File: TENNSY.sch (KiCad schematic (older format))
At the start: 24 parts, among them J1 HEADER_2, J2 HEADER_2, U1 Teensy4.0, U2 DRV8872, U3 QRE1113, U4 QRE1113, U5 QRE1113, U6 QRE1113, U7 QRE1113, U8 DRV8872

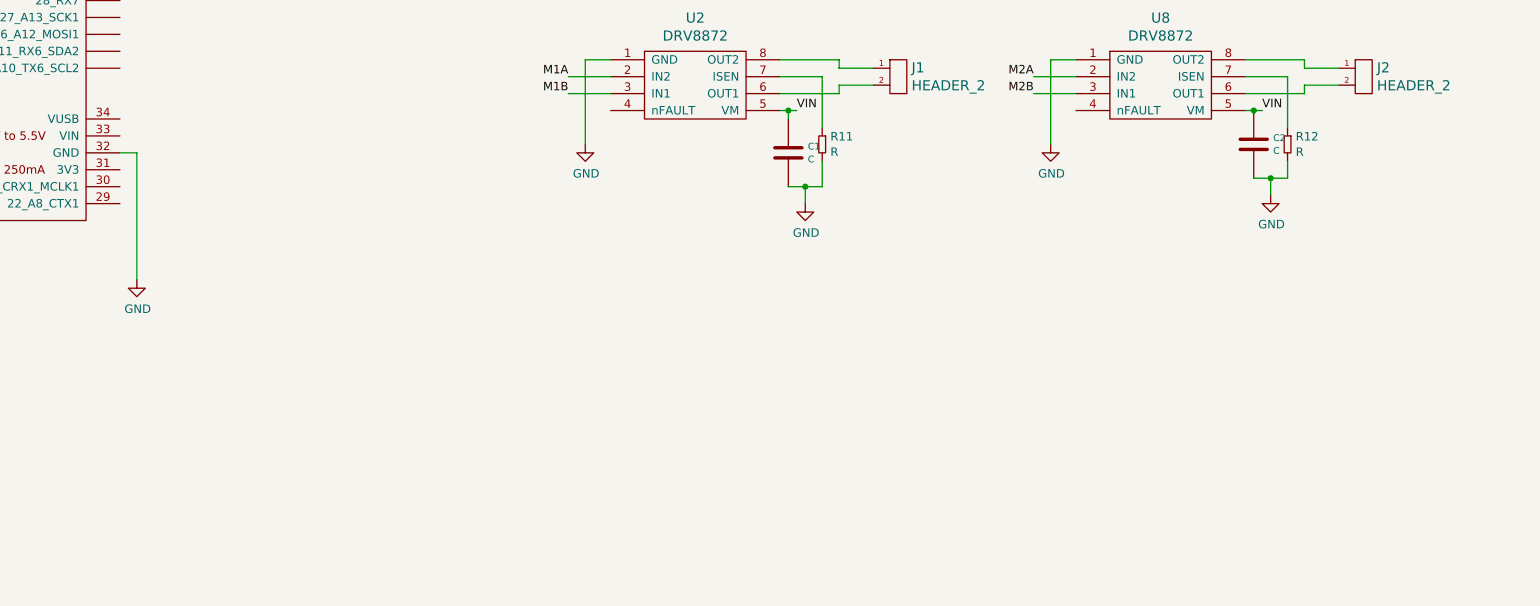
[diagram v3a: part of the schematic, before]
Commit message: modificaciones
se modifico sch,pcb:
se agrego una llave
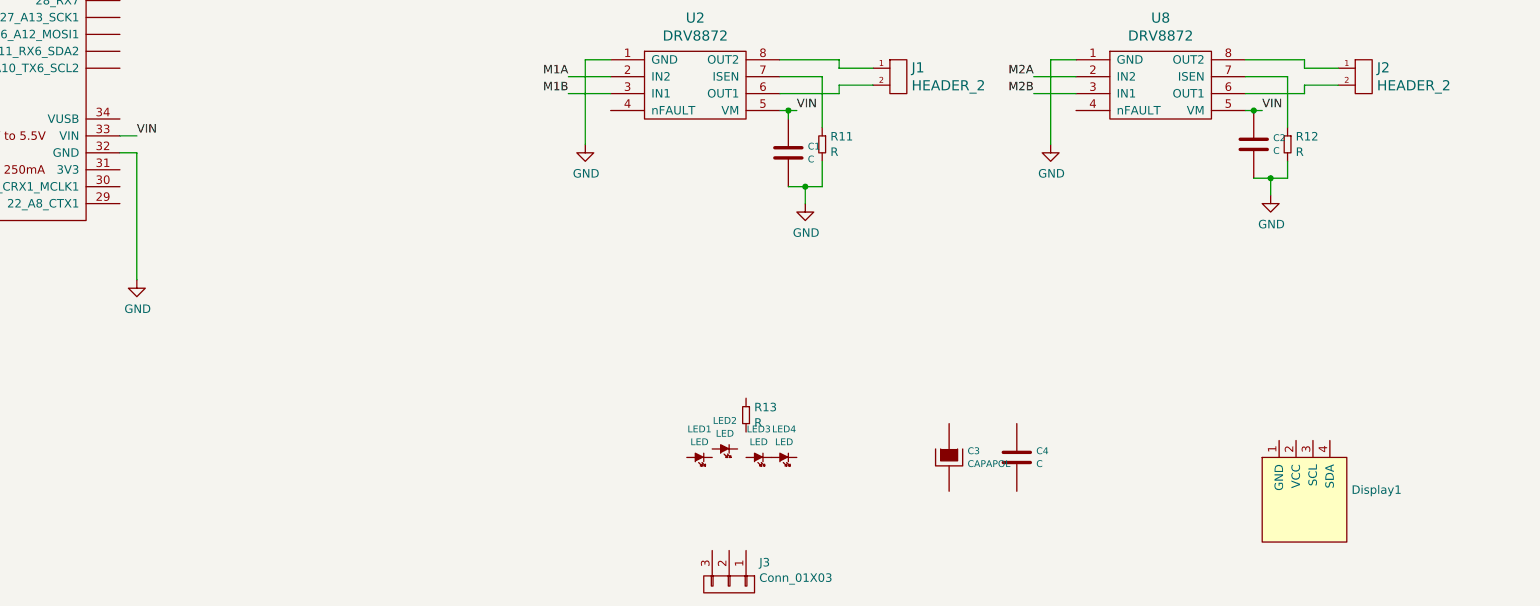
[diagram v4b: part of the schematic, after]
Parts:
- added C3: CAPAPOL, symbol EESTN5:CAPAPOL
- added C4: C, symbol EESTN5:C
- added Display1: SSD1306-SSD1306-128x64_OLED, EESTN5:128x64OLED, symbol EESTN5:SSD1306-SSD1306-128x64_OLED
- added J3: Conn_01X03, Button_Switch_SMD:SW_SPDT_PCM12, symbol EESTN5:Conn_01X03
- added LED1, LED2, LED3, LED4: LED, symbol EESTN5:LED
- added R13: R, symbol EESTN5:R
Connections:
- net VIN: now also U1.33 (VIN)
- new net: LED3.2 (K), LED4.1 (A)
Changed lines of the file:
@@
 Wire Wire Line
 	9950 3200 10000 3200
+Wire Wire Line
+	3250 3350 3350 3350
+Text Label 3350 3350 0    50   ~ 0
+VIN
+$Comp
+L EESTN5:SSD1306-SSD1306-128x64_OLED Display1
+U 1 1 60E7DE53
+P 10250 5500
+F 0 "Display1" H 10528 5558 50  0000 L CNN
+F 1 "SSD1306-SSD1306-128x64_OLED" H 10250 5450 50  0001 C CNN
+F 2 "EESTN5:128x64OLED" H 10250 5750 50  0001 C CNN
+F 3 "" H 10250 5750 50  0001 C CNN
+	1    10250 5500
+	1    0    0    -1
+$EndComp
+$Comp
+L EESTN5:C C4
+U 1 1 60E7E7AF
+P 8550 5250
+F 0 "C4" H 8665 5288 40  0000 L CNN
+F 1 "C" H 8665 5212 40  0000 L CNN
+F 2 "" H 8588 5100 30  0001 C CNN
+F 3 "" H 8550 5250 60  0000 C CNN
+	1    8550 5250
+	1    0    0    -1
+$EndComp
+$Comp
+L EESTN5:CAPAPOL C3
+U 1 1 60E7EE1B
+P 8150 5250
+F 0 "C3" H 8259 5288 40  0000 L CNN
+F 1 "CAPAPOL" H 8259 5212 40  0000 L CNN
+F 2 "" H 8250 5100 30  0001 C CNN
+F 3 "" H 8150 5250 300 0000 C CNN
+	1    8150 5250
+	1    0    0    -1
+$EndComp
+$Comp
+L EESTN5:LED LED1
+U 1 1 60E7F5B7
+P 6650 5250
+F 0 "LED1" H 6675 5417 40  0000 C CNN
+F 1 "LED" H 6675 5341 40  0000 C CNN
+F 2 "" H 6650 5250 60  0001 C CNN
+F 3 "" H 6650 5250 60  0000 C CNN
+	1    6650 5250
+	1    0    0    -1
+$EndComp
+$Comp
+L EESTN5:R R13
+U 1 1 60E7FA33
+P 6950 5000
+F 0 "R13" H 6998 5046 50  0000 L CNN
+F 1 "R" H 6998 4955 50  0000 L CNN
+F 2 "" H 6950 5000 60  0001 C CNN
+F 3 "" H 6950 5000 60  0000 C CNN
+	1    6950 5000
+	1    0    0    -1
+$EndComp
+$Comp
+L EESTN5:LED LED2
+U 1 1 60E80025
+P 6800 5200
+F 0 "LED2" H 6825 5367 40  0000 C CNN
+F 1 "LED" H 6825 5291 40  0000 C CNN
+F 2 "" H 6800 5200 60  0001 C CNN
+F 3 "" H 6800 5200 60  0000 C CNN
+	1    6800 5200
+	1    0    0    -1
+$EndComp
+$Comp
+L EESTN5:LED LED3
+U 1 1 60E80C4D
+P 7000 5250
+F 0 "LED3" H 7025 5417 40  0000 C CNN
+F 1 "LED" H 7025 5341 40  0000 C CNN
+F 2 "" H 7000 5250 60  0001 C CNN
+F 3 "" H 7000 5250 60  0000 C CNN
+	1    7000 5250
+	1    0    0    -1
+$EndComp
+$Comp
+L EESTN5:LED LED4
+U 1 1 60E814F3
+P 7150 5250
+F 0 "LED4" H 7175 5417 40  0000 C CNN
+F 1 "LED" H 7175 5341 40  0000 C CNN
+F 2 "" H 7150 5250 60  0001 C CNN
+F 3 "" H 7150 5250 60  0000 C CNN
+	1    7150 5250
+	1    0    0    -1
+$EndComp
+$Comp
+L EESTN5:Conn_01X03 J3
+U 1 1 60E81E46
+P 6850 6000
+F 0 "J3" V 6721 6178 50  0000 L CNN
+F 1 "Conn_01X03" V 6812 6178 50  0000 L CNN
+F 2 "Button_Switch_SMD:SW_SPDT_PCM12" H 6850 6000 50  0001 C CNN
+F 3 "" H 6850 6000 50  0001 C CNN
+	1    6850 6000
+	0    1    1    0
+$EndComp
 $EndSCHEMATC

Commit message: MODIFICACIONES
se modifico el sch y pcb
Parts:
- added J4: TB_1X2, EESTN5:BORNERA2_DUO, symbol EESTN5:TB_1X2
- added Q1, Q2, Q3: 2N7002, EESTN5:SOT23, symbol EESTN5:2N7002
- added R14, R15, R16, R17, R18, R19, R20, R21: R, EESTN5:R_1206, symbol EESTN5:R
- added SW1: SW_DIP_x02, EESTN5:DIP-4_PC817, symbol EESTN5:SW_DIP_x02
- C3: footprint (none) -> EESTN5:CAP_ELEC_SMD_4X5.5
- C4: footprint (none) -> EESTN5:C_1206
- LED1, LED2, LED3, LED4: footprint (none) -> EESTN5:LED_1206
- R13: footprint (none) -> EESTN5:R_1206
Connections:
- net GND: now also C3.2, C4.2, Display1.1 (GND), R13.2, J4.1, Q1.3 (S), Q2.3 (S), Q3.3 (S), R15.2, R16.2, R18.2, SW1.3, SW1.4
- net M1A: now also U1.4 (2_OUT2)
- net M1B: now also U1.5 (3_LRCLK2)
- net M2A: now also U1.7 (5_IN2)
- net M2B: now also U1.8 (6_OUT1D)
- net MODO2: now reaches U1.10 (8_TX2_IN1)
- net MODO2: now also Q2.1 (G), R16.1
- net MODO3: now reaches U1.11 (9_OUT1C)
- net MODO3: now also Q3.1 (G), R18.1
- net SDA: now reaches U1.25 (18_A4_SDA0)
- net SDA: now also Display1.4 (SDA)
- net SCL: now reaches U1.26 (19_A5_SCL0)
- net SCL: now also Display1.3 (SCL)
- net MODE1: now reaches U1.9 (7_RX2_OUT1A)
- net MODE1: now also R13.1, Q1.1 (G)
- net VCC: now reaches Display1.2 (VCC)
- net VCC: now also LED1.2 (K), LED2.2 (K), LED4.2 (K), R20.1, R21.1
- net at C4.1: now also C3.1, J3.1 (P1), LED3.1 (A)
- net at LED1.1 (A): now also R19.1
- net at LED2.1 (A): now also R17.1
- net at LED3.2 (K): now also R15.1; no longer LED4.1 (A)
- net at J3.2 (P2): now also J3.3 (P3), J4.2
- new net: LED4.1 (A), R14.1
- new net: Q1.2 (D), R14.2
- new net: Q2.2 (D), R17.2
- new net: Q3.2 (D), R19.2
- new net ESTRATEGIAS1: R20.2, SW1.2
- new net ESTRATEGIAS2: R21.2, SW1.1
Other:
- moved on the sheet: C3, C4, Display1, J3, LED1, LED2, LED3, LED4, R13

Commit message: modificaciones
se realizo modificaciones en el sch y pcb, proyecto en su 70% para su finalizacion
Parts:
- added C5: C, EESTN5:C_1206, symbol EESTN5:C
- added U9: LM1117-SOT, EESTN5:SOT223, symbol EESTN5:LM1117-SOT
- J3: footprint Button_Switch_SMD:SW_SPDT_PCM12 -> EESTN5:Pin_Strip_3
- SW1: footprint EESTN5:DIP-4_PC817 -> EESTN5:Dip_SW_2-300
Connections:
- net GND: now also C5.2, U9.1 (ADJ/GND)
- net M1A: now also U2.3 (IN1); no longer U2.2 (IN2)
- net M1B: now also U2.2 (IN2); no longer U2.3 (IN1)
- net M2A: now also U8.3 (IN1); no longer U8.2 (IN2)
- net M2B: now also U8.2 (IN2); no longer U8.3 (IN1)
- net VCC: now also U1.33 (VIN), C5.1, U9.2 (VOUT), U9.4 (VOUT)
- net VIN: no longer U1.33 (VIN)
- net at C3.1, C4.1, J3.1 (P1)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: now also U9.3 (VIN)
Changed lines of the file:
@@
 Wire Wire Line
 	6000 2900 6000 3400
-Text Label 5900 3000 2    50   ~ 0
-M1A
 Text Label 5900 3100 2    50   ~ 0
+M1A
+Text Label 5900 3000 2    50   ~ 0
 M1B
 $Comp
@@
 Wire Wire Line
 	8750 2900 8750 3400
-Text Label 8650 3000 2    50   ~ 0
-M2A
 Text Label 8650 3100 2    50   ~ 0
+M2A
+Text Label 8650 3000 2    50   ~ 0
 M2B
 $Comp
@@
 U 1 1 60E9E604
 P 7200 3450
-F 0 "C1" H 7315 3488 40  0000 L CNN
-F 1 "C" H 7315 3412 40  0000 L CNN
+F 0 "C1" H 7000 3500 40  0000 L CNN
+F 1 "C" H 7000 3400 40  0000 L CNN
 F 2 "EESTN5:CAP_ELEC_SMD_4X5.5" H 7238 3300 30  0001 C CNN
 F 3 "" H 7200 3450 60  0000 C CNN
@@
 U 1 1 60EAB8A9
 P 9950 3400
-F 0 "C2" H 10065 3438 40  0000 L CNN
-F 1 "C" H 10065 3362 40  0000 L CNN
+F 0 "C2" H 9750 3450 40  0000 L CNN
+F 1 "C" H 9750 3350 40  0000 L CNN
 F 2 "EESTN5:CAP_ELEC_SMD_4X5.5" H 9988 3250 30  0001 C CNN
 F 3 "" H 9950 3400 60  0000 C CNN
@@
 Wire Wire Line
 	9950 3200 10000 3200
-Wire Wire Line
-	3250 3350 3350 3350
-Text Label 3350 3350 0    50   ~ 0
-VIN
 $Comp
 L EESTN5:SSD1306-SSD1306-128x64_OLED Display1
 U 1 1 60E7DE53
 P 10750 5600
-F 0 "Display1" H 11028 5658 50  0000 L CNN
+F 0 "Display1" H 10650 5250 50  0000 L CNN
 F 1 "SSD1306-SSD1306-128x64_OLED" H 10750 5550 50  0001 C CNN
 F 2 "EESTN5:128x64OLED" H 10750 5850 50  0001 C CNN
@@
 U 1 1 60E7EE1B
 P 1750 5700
-F 0 "C3" H 1859 5738 40  0000 L CNN
-F 1 "CAPAPOL" H 1859 5662 40  0000 L CNN
+F 0 "C3" H 1650 5800 40  0000 L CNN
+F 1 "CAPAPOL" H 1600 5600 40  0000 L CNN
 F 2 "EESTN5:CAP_ELEC_SMD_4X5.5" H 1850 5550 30  0001 C CNN
 F 3 "" H 1750 5700 300 0000 C CNN
@@
 U 1 1 60E7F5B7
 P 3600 6300
-F 0 "LED1" H 3625 6467 40  0000 C CNN
-F 1 "LED" H 3625 6391 40  0000 C CNN
+F 0 "LED1" V 3700 6450 40  0000 C CNN
+F 1 "LED" V 3600 6450 40  0000 C CNN
 F 2 "EESTN5:LED_1206" H 3600 6300 60  0001 C CNN
 F 3 "" H 3600 6300 60  0000 C CNN
@@
 U 1 1 60E80025
 P 2450 6300
-F 0 "LED2" H 2475 6467 40  0000 C CNN
-F 1 "LED" H 2475 6391 40  0000 C CNN
+F 0 "LED2" V 2550 6450 40  0000 C CNN
+F 1 "LED" V 2450 6450 40  0000 C CNN
 F 2 "EESTN5:LED_1206" H 2450 6300 60  0001 C CNN
 F 3 "" H 2450 6300 60  0000 C CNN
@@
 U 1 1 60E80C4D
 P 1850 5350
-F 0 "LED3" H 1875 5517 40  0000 C CNN
-F 1 "LED" H 1875 5441 40  0000 C CNN
+F 0 "LED3" V 2000 5250 40  0000 C CNN
+F 1 "LED" V 1900 5200 40  0000 C CNN
 F 2 "EESTN5:LED_1206" H 1850 5350 60  0001 C CNN
 F 3 "" H 1850 5350 60  0000 C CNN
@@
 U 1 1 60E81E46
 P 1450 5700
-F 0 "J3" V 1321 5878 50  0000 L CNN
-F 1 "Conn_01X03" V 1412 5878 50  0000 L CNN
-F 2 "Button_Switch_SMD:SW_SPDT_PCM12" H 1450 5700 50  0001 C CNN
+F 0 "J3" V 1550 5650 50  0000 L CNN
+F 1 "Conn_01X03" V 1100 5450 50  0000 L CNN
+F 2 "EESTN5:Pin_Strip_3" H 1450 5700 50  0001 C CNN
 F 3 "" H 1450 5700 50  0001 C CNN
 	1    1450 5700
@@
 U 1 1 60E814F3
 P 1200 6300
-F 0 "LED4" H 1225 6467 40  0000 C CNN
-F 1 "LED" H 1225 6391 40  0000 C CNN
+F 0 "LED4" V 1300 6450 40  0000 C CNN
+F 1 "LED" V 1200 6450 40  0000 C CNN
 F 2 "EESTN5:LED_1206" H 1200 6300 60  0001 C CNN
 F 3 "" H 1200 6300 60  0000 C CNN
@@
 F 0 "SW1" V 4754 7180 50  0000 L CNN
 F 1 "SW_DIP_x02" V 4845 7180 50  0000 L CNN
-F 2 "EESTN5:DIP-4_PC817" H 4800 6950 50  0001 C CNN
+F 2 "EESTN5:Dip_SW_2-300" H 4800 6950 50  0001 C CNN
 F 3 "" H 4800 6950 50  0001 C CNN
 	1    4800 6950
@@
 $EndComp
 $Comp
-L EESTN5:R R20
-U 1 1 60EFAC6F
-P 4800 6400
-F 0 "R20" H 4848 6446 50  0000 L CNN
-F 1 "R" H 4848 6355 50  0000 L CNN
-F 2 "EESTN5:R_1206" H 4800 6400 60  0001 C CNN
-F 3 "" H 4800 6400 60  0000 C CNN
-	1    4800 6400
-	1    0    0    -1
-$EndComp
-$Comp
 L EESTN5:R R21
 U 1 1 60EFB24F
 P 4900 6400
-F 0 "R21" H 4948 6446 50  0000 L CNN
-F 1 "R" H 4948 6355 50  0000 L CNN
+F 0 "R21" H 4950 6500 50  0000 L CNN
+F 1 "R" H 4950 6400 50  0000 L CNN
 F 2 "EESTN5:R_1206" H 4900 6400 60  0001 C CNN
 F 3 "" H 4900 6400 60  0000 C CNN
@@
 Text Label 850  2050 2    50   ~ 0
 MODO3
+$Comp
+L EESTN5:R R20
+U 1 1 60EFAC6F
+P 4800 6400
+F 0 "R20" H 4600 6500 50  0000 L CNN
+F 1 "R" H 4650 6400 50  0000 L CNN
+F 2 "EESTN5:R_1206" H 4800 6400 60  0001 C CNN
+F 3 "" H 4800 6400 60  0000 C CNN
+	1    4800 6400
+	1    0    0    -1
+$EndComp
+$Comp
+L EESTN5:LM1117-SOT U9
+U 1 1 60F4CF42
+P 2850 5450
+F 0 "U9" H 2850 5807 60  0000 C CNN
+F 1 "LM1117-SOT" H 2850 5701 60  0000 C CNN
+F 2 "EESTN5:SOT223" H 2850 5450 60  0001 C CNN
+F 3 "http://www.mouser.com/ds/2/282/lm1117-n-7107.pdf" H 2850 5595 60  0000 C CNN
+	1    2850 5450
+	1    0    0    -1
+$EndComp
+Wire Wire Line
+	2500 5450 2000 5450
+Connection ~ 2000 5450
+Wire Wire Line
+	2850 5800 2850 5900
+$Comp
+L power:GND #PWR0132
+U 1 1 60F67818
+P 2850 5900
+F 0 "#PWR0132" H 2850 5650 50  0001 C CNN
+F 1 "GND" H 2855 5727 50  0000 C CNN
+F 2 "" H 2850 5900 50  0001 C CNN
+F 3 "" H 2850 5900 50  0001 C CNN
+	1    2850 5900
+	1    0    0    -1
+$EndComp
+Wire Wire Line
+	3200 5450 3350 5450
+Wire Wire Line
+	3350 5450 3350 5500
+Wire Wire Line
+	3350 5550 3200 5550
+Connection ~ 3350 5500
+Wire Wire Line
+	3350 5500 3350 5550
+$Comp
+L EESTN5:C C5
+U 1 1 60F81E1E
+P 3850 5750
+F 0 "C5" H 3965 5788 40  0000 L CNN
+F 1 "C" H 3965 5712 40  0000 L CNN
+F 2 "EESTN5:C_1206" H 3888 5600 30  0001 C CNN
+F 3 "" H 3850 5750 60  0000 C CNN
+	1    3850 5750
+	1    0    0    -1
+$EndComp
+Wire Wire Line
+	3850 5550 3850 5500
+Wire Wire Line
+	3350 5500 3850 5500
+Wire Wire Line
+	3850 5500 4200 5500
+Wire Wire Line
+	4200 5500 4200 5350
+Connection ~ 3850 5500
+Wire Wire Line
+	3850 5950 3850 6050
+$Comp
+L power:GND #PWR0133
+U 1 1 60FAC810
+P 3850 6050
+F 0 "#PWR0133" H 3850 5800 50  0001 C CNN
+F 1 "GND" H 3855 5877 50  0000 C CNN
+F 2 "" H 3850 6050 50  0001 C CNN
+F 3 "" H 3850 6050 50  0001 C CNN
+	1    3850 6050
+	1    0    0    -1
+$EndComp
+$Comp
+L power:VCC #PWR0134
+U 1 1 60FACE5E
+P 4200 5350
+F 0 "#PWR0134" H 4200 5200 50  0001 C CNN
+F 1 "VCC" H 4217 5523 50  0000 C CNN
+F 2 "" H 4200 5350 50  0001 C CNN
+F 3 "" H 4200 5350 50  0001 C CNN
+	1    4200 5350
+	1    0    0    -1
+$EndComp
+Wire Wire Line
+	3500 3350 3500 3200
+Wire Wire Line
+	3250 3350 3500 3350
+$Comp
+L power:VCC #PWR0135
+U 1 1 60FBBEEB
+P 3500 3200
+F 0 "#PWR0135" H 3500 3050 50  0001 C CNN
+F 1 "VCC" H 3517 3373 50  0000 C CNN
+F 2 "" H 3500 3200 50  0001 C CNN
+F 3 "" H 3500 3200 50  0001 C CNN
+	1    3500 3200
+	1    0    0    -1
+$EndComp
 $EndSCHEMATC
